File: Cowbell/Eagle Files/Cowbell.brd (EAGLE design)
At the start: 100 x 50 mm, 75 parts, among them IC1 LM741P, Q1 2N3906, T1 2N3904, T2 2N3904, T3 2N3904, T4 2N3904, T5 2N3904, T6 2N3904, T7 2N3904, T8 2N3904

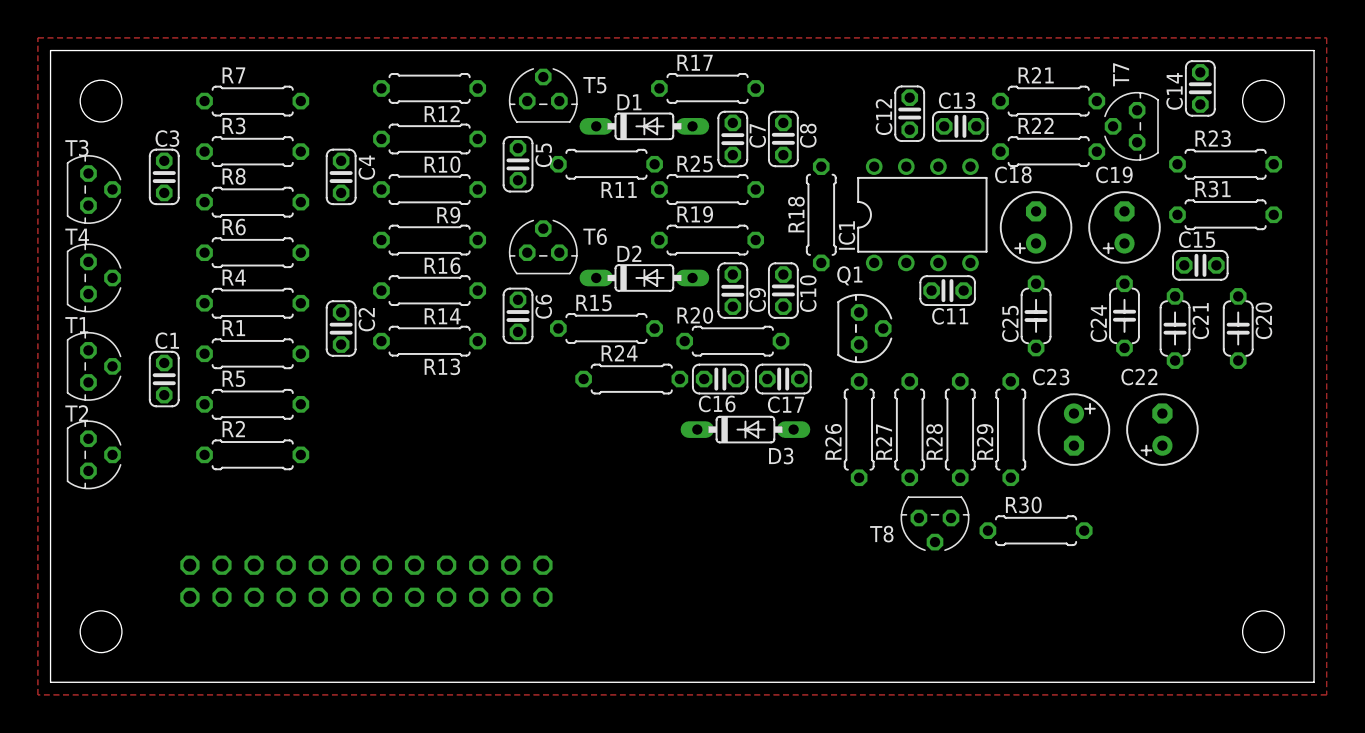
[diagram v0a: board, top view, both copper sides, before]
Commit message: Completed board layout, generated CAM files, and organized files and folders.
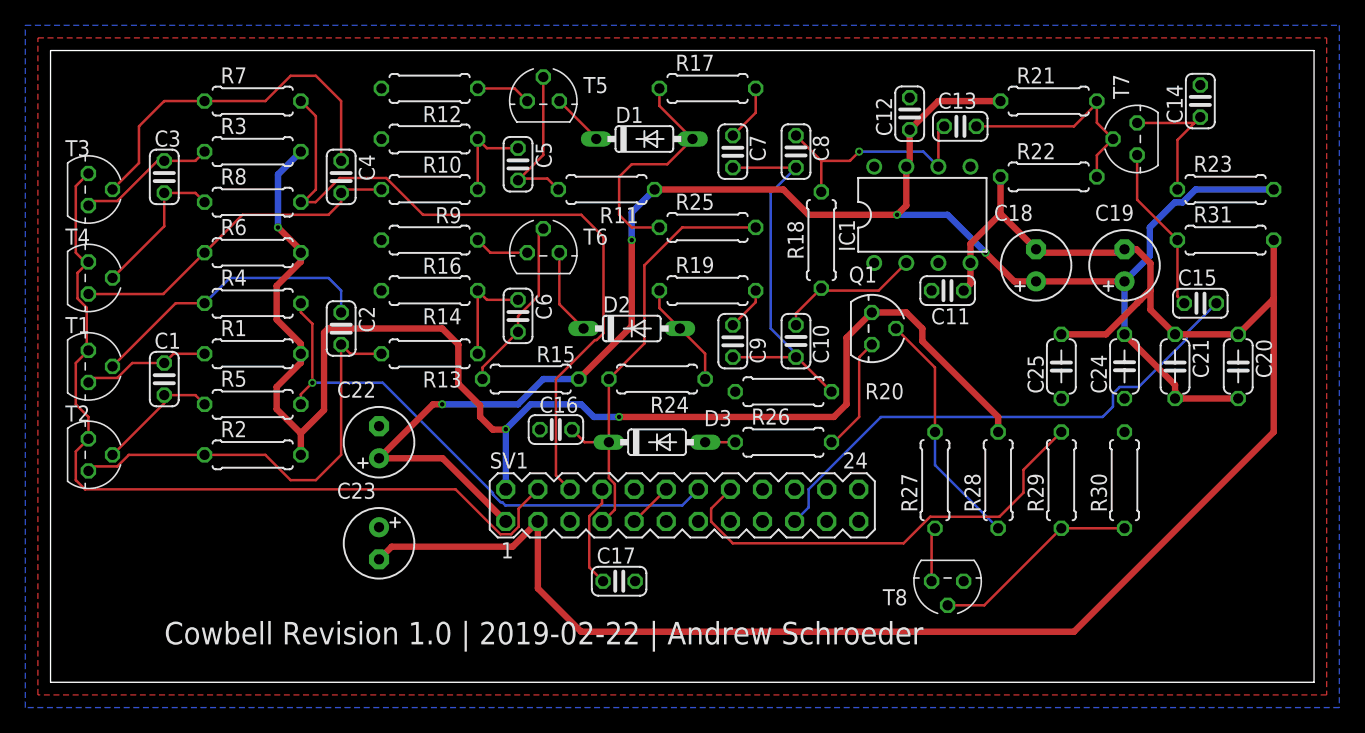
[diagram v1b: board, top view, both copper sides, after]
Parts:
- removed U$1, U$2, U$3, U$4: (no value), ARVP:STAND-OFF
- removed U$5: (no value), frames:A4L-LOC
- added U$6: (no value), frames:A5L-LOC
- moved C22 62.0 mm to (26.0, 19.0)
- moved C23 55.7 mm to (26.0, 11.0)
- moved SV1 25.7 mm to (50.0, 14.0), flipped to the top, turned to 0 degrees
- moved C17 20.6 mm to (45.0, 8.00), turned to 0 degrees
- moved C16 13.6 mm to (40.0, 20.0), turned to 180 degrees
- moved R30 8.06 mm to (85.0, 16.0), turned to 270 degrees
- moved R15 7.21 mm to (38.0, 24.0), turned to 180 degrees
- moved D3 7.07 mm to (48.0, 19.0)
- moved R26 6.08 mm to (58.0, 19.0), turned to 0 degrees
- moved R20 5.66 mm to (58.0, 23.0)
- moved R29 5.66 mm to (80.0, 16.0)
- moved T8 5.10 mm to (71.0, 8.00)
- moved R28 5.00 mm to (75.0, 16.0)
- moved C25 4.47 mm to (80.0, 25.0)
- moved R27 4.47 mm to (70.0, 16.0)
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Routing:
- net -12V: track 0.00 -> 148.5 mm
- net +12V: track 0.00 -> 135.8 mm, vias 0 -> 4
- net +5V: track 0.00 -> 114.3 mm, vias 0 -> 3
- net DGND: track 0.00 -> 67.9 mm
- net POT1: track 0.00 -> 57.8 mm
- net POT9: track 0.00 -> 43.9 mm, vias 0 -> 1
- net OUTPUT: track 0.00 -> 42.3 mm
- net TRIGGER: track 0.00 -> 36.3 mm
- net POT4: track 0.00 -> 35.5 mm
- net N$2: track 0.00 -> 34.4 mm
- net N$21: track 0.00 -> 30.6 mm
- net N$6: track 0.00 -> 29.1 mm
- net N$1: track 0.00 -> 27.0 mm
- net N$4: track 0.00 -> 23.1 mm
- net N$39: track 0.00 -> 19.2 mm
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- added copper zone on layer 16, net GND
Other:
- board text added: "Cowbell Revision 1.0 | 2019-02-22 | Andrew Schroeder"

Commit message: cleanup
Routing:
- net -12V: track 148.5 -> 150.2 mm
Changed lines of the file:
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@@
 <?xml version="1.0" encoding="utf-8"?>
 <!DOCTYPE eagle SYSTEM "eagle.dtd">
-<eagle version="9.2.2">
+<eagle version="9.3.1">
 <drawing>
 <settings>
@@
 </class>
 </classes>
-<designrules name="JLCPCB2Layer">
+<designrules name="SeeedStudio_2layer_DRU_no_angle_20140221">
 <description language="de">&lt;b&gt;EAGLE Design Rules&lt;/b&gt;
 &lt;p&gt;
@@
 </description>
 <param name="layerSetup" value="(1*16)"/>
-<param name="mtCopper" value="0.035mm 0.035mm 0.035mm 0.035mm 0.035mm 0.035mm 0.035mm 0.035mm 0.035mm 0.035mm 0.035mm 0.035mm 0.035mm 0.035mm 0.035mm 0.035mm"/>
-<param name="mtIsolate" value="1.5mm 0.15mm 0.2mm 0.15mm 0.2mm 0.15mm 0.2mm 0.15mm 0.2mm 0.15mm 0.2mm 0.15mm 0.2mm 0.15mm 0.2mm"/>
+<param name="mtCopper" value="0.035mm 0.0175mm 0.035mm 0.035mm 0.035mm 0.035mm 0.035mm 0.035mm 0.035mm 0.035mm 0.035mm 0.035mm 0.035mm 0.035mm 0.0175mm 0.035mm"/>
+<param name="mtIsolate" value="1.5mm 1.1mm 0.2mm 0.15mm 0.2mm 0.15mm 0.2mm 0.15mm 0.2mm 0.15mm 0.2mm 0.15mm 0.2mm 0.15mm 0.2mm"/>
 <param name="mdWireWire" value="6mil"/>
 <param name="mdWirePad" value="6mil"/>
@@
 <param name="mdSmdStop" value="0mil"/>
 <param name="msWidth" value="6mil"/>
-<param name="msDrill" value="10mil"/>
-<param name="msMicroVia" value="10mil"/>
+<param name="msDrill" value="12mil"/>
+<param name="msMicroVia" value="12mil"/>
 <param name="msBlindViaRatio" value="0.5"/>
 <param name="rvPadTop" value="0.25"/>
@@
 <param name="rvMicroViaOuter" value="0.25"/>
 <param name="rvMicroViaInner" value="0.25"/>
-<param name="rlMinPadTop" value="6mil"/>
+<param name="rlMinPadTop" value="10mil"/>
 <param name="rlMaxPadTop" value="20mil"/>
-<param name="rlMinPadInner" value="6mil"/>
+<param name="rlMinPadInner" value="10mil"/>
 <param name="rlMaxPadInner" value="20mil"/>
-<param name="rlMinPadBottom" value="6mil"/>
+<param name="rlMinPadBottom" value="10mil"/>
 <param name="rlMaxPadBottom" value="20mil"/>
 <param name="rlMinViaOuter" value="6mil"/>
@@
 <wire x1="46" y1="37.19" x2="47.81" y2="39" width="0.508" layer="16"/>
 <wire x1="85" y1="31.73" x2="85" y2="27.54" width="0.508" layer="16"/>
-<wire x1="90.62684375" y1="39" x2="96.81" y2="39" width="0.508" layer="16"/>
+<wire x1="93.02684375" y1="39" x2="96.81" y2="39" width="0.508" layer="16"/>
 <wire x1="31.03" y1="17.73" x2="36.03" y2="12.73" width="0.508" layer="1"/>
 <wire x1="31.03" y1="17.73" x2="26" y2="17.73" width="0.508" layer="1"/>
@@
 <wire x1="85" y1="31.73" x2="87" y2="33.73" width="0.508" layer="16"/>
 <wire x1="87" y1="33.73" x2="87" y2="36" width="0.508" layer="16"/>
-<wire x1="87" y1="36" x2="88.984" y2="37.984" width="0.508" layer="16"/>
-<wire x1="88.984" y1="37.984" x2="89.61084375" y2="37.984" width="0.508" layer="16"/>
-<wire x1="89.61084375" y1="37.984" x2="90.62684375" y2="39" width="0.508" layer="16"/>
+<wire x1="87" y1="36" x2="87.984" y2="36.984" width="0.508" layer="16"/>
+<wire x1="87.984" y1="36.984" x2="91.01084375" y2="36.984" width="0.508" layer="16"/>
+<wire x1="91.01084375" y1="36.984" x2="93.02684375" y2="39" width="0.508" layer="16"/>
 </signal>
 <signal name="-12V">
@@
 <wire x1="89" y1="27.54" x2="87.0525" y2="29.4875" width="0.508" layer="1"/>
 <wire x1="85" y1="34" x2="85" y2="34.27" width="0.2" layer="1"/>
-<wire x1="87.0525" y1="29.4875" x2="87.0525" y2="31" width="0.508" layer="1"/>
-<wire x1="87.0525" y1="31" x2="87.0525" y2="33.1659625" width="0.508" layer="1"/>
+<wire x1="87.0525" y1="29.4875" x2="87.0525" y2="30" width="0.508" layer="1"/>
+<wire x1="87.0525" y1="30" x2="87.0525" y2="31" width="0.508" layer="1"/>
+<wire x1="87.0525" y1="31" x2="87.0525" y2="31.3525" width="0.508" layer="1"/>
+<wire x1="87.0525" y1="32" x2="87.0525" y2="33.1659625" width="0.508" layer="1"/>
 <wire x1="87.0525" y1="33.1659625" x2="85.9484625" y2="34.27" width="0.508" layer="1"/>
 <wire x1="85" y1="34.27" x2="85.9484625" y2="34.27" width="0.508" layer="1"/>
-<wire x1="80" y1="27.54" x2="83.54" y2="27.54" width="0.508" layer="1"/>
-<wire x1="83.54" y1="27.54" x2="86" y2="30" width="0.508" layer="1"/>
-<wire x1="86" y1="30" x2="86.27" y2="30.27" width="0.508" layer="1"/>
+<wire x1="80" y1="27.54" x2="83.24" y2="27.54" width="0.508" layer="1"/>
 <wire x1="75.19" y1="40" x2="75.19" y2="37.08" width="0.508" layer="1"/>
 <wire x1="75.19" y1="37.08" x2="78" y2="34.27" width="0.508" layer="1"/>
@@
 <wire x1="96.81" y1="19.81" x2="96.81" y2="30.35" width="0.508" layer="1"/>
 <wire x1="38.57" y1="7.43" x2="42" y2="4" width="0.508" layer="1"/>
-<wire x1="86.27" y1="30.27" x2="87" y2="31" width="0.508" layer="1"/>
-<wire x1="87" y1="31" x2="87.0525" y2="31" width="0.508" layer="1"/>
+<wire x1="83.24" y1="27.54" x2="85.85" y2="30.15" width="0.508" layer="1"/>
+<wire x1="85.85" y1="30.15" x2="86.55" y2="30.85" width="0.508" layer="1"/>
+<wire x1="86.55" y1="30.85" x2="86.7" y2="31" width="0.508" layer="1"/>
+<wire x1="86.7" y1="31" x2="87.0525" y2="31" width="0.508" layer="1"/>
+<wire x1="87.0525" y1="30" x2="86.55" y2="30.5025" width="0.508" layer="1"/>
+<wire x1="86.55" y1="30.5025" x2="86.55" y2="30.85" width="0.508" layer="1"/>
+<wire x1="86.55" y1="30.85" x2="87.0525" y2="31.3525" width="0.508" layer="1"/>
+<wire x1="87.0525" y1="31.3525" x2="87.0525" y2="32" width="0.508" layer="1"/>
 </signal>
 <signal name="OUTPUT">
@@
 <wire x1="2" y1="16" x2="2" y2="18.27" width="0.2" layer="1"/>
 <wire x1="2" y1="18.27" x2="3" y2="19.27" width="0.2" layer="1"/>
-<wire x1="2.865" y1="29.64594375" x2="2.865" y2="26.135" width="0.2" layer="1"/>
-<wire x1="2.138" y1="30.37294375" x2="2.865" y2="29.64594375" width="0.2" layer="1"/>
-<wire x1="2.138" y1="32.408" x2="2.138" y2="30.37294375" width="0.2" layer="1"/>
+<wire x1="2.865" y1="29.54594375" x2="2.865" y2="26.135" width="0.2" layer="1"/>
+<wire x1="2.038" y1="30.37294375" x2="2.865" y2="29.54594375" width="0.2" layer="1"/>
+<wire x1="2.038" y1="32.308" x2="2.038" y2="30.37294375" width="0.2" layer="1"/>
 <wire x1="3" y1="33.27" x2="2.865" y2="33.135" width="0.2" layer="1"/>
-<wire x1="2.865" y1="33.135" x2="2.138" y2="32.408" width="0.2" layer="1"/>
+<wire x1="2.865" y1="33.135" x2="2.038" y2="32.308" width="0.2" layer="1"/>
 <wire x1="3" y1="40.27" x2="2" y2="39.27" width="0.2" layer="1"/>
 <wire x1="2" y1="34" x2="2.865" y2="33.135" width="0.2" layer="1"/>
